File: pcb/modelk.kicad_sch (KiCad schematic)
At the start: 40 parts, among them J1 JST-PH connector, J2 Conn_01x20, J3 User exposed, J4 Conn_01x12, J5 Conn_01x04, J6 Conn_01x08, J7 Faston PCB mount, J8 Dupont for power profiling, SW1 SW_reset, U1 nice_nano, U2 74HC595, U3 74HC595, U4 74HC595

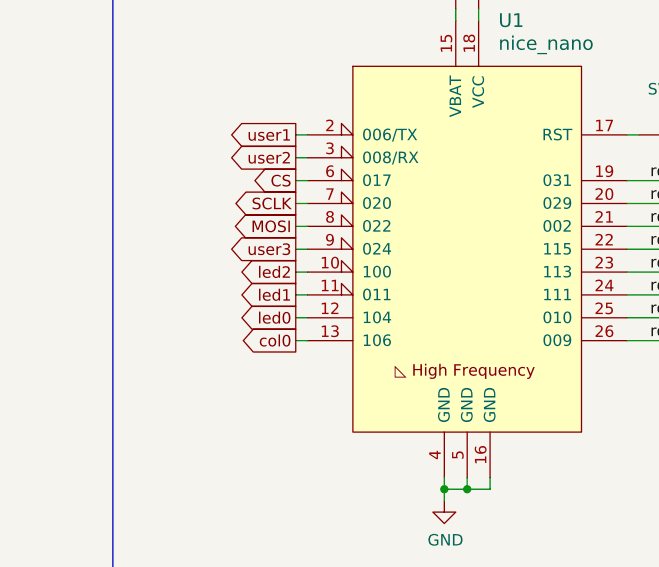
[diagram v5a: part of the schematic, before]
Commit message: All leds on high frequency pins
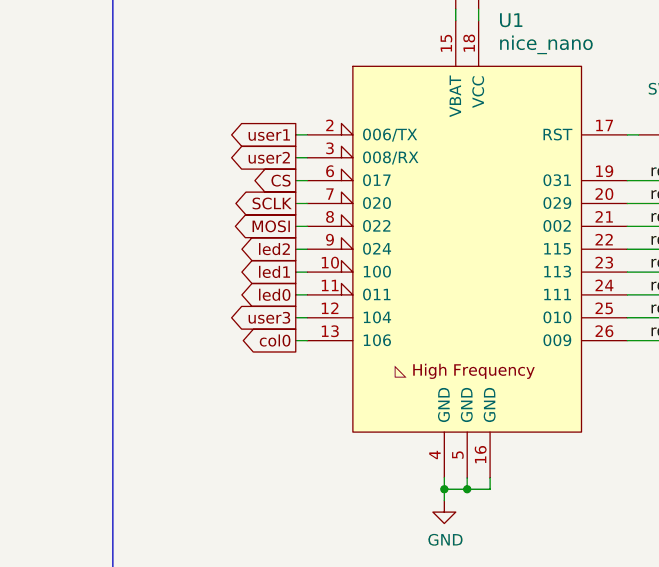
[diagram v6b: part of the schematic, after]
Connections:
- net led0: now also U1.11 (011); no longer U1.12 (104)
- net led1: now also U1.10 (100); no longer U1.11 (011)
- net led2: now also U1.9 (024); no longer U1.10 (100)
- net user3: now also U1.12 (104); no longer U1.9 (024)
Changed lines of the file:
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@@
 		(title "Model K")
 		(date "2025-06-15")
-		(rev "0.7.4")
+		(rev "0.7.5")
 	)
 	(rectangle
@@
 			"AAAAAAAAAAAAAAAAAAAAAAAAAAAAAAAAAAAAAAAAAAAAAAAAAAAAAAAAAAAAAAAAAAAAAAAAAAAA"
 			"AAAAAAAAAAAAAAAAAND29EoAAAAA0Pb0SgAAAAAAAAAAAAAAAAAAAAAAAAAAAAAAAAAAAAAAAAAA"
+			"AAAAAAAAAAAAAAAAAAAAAAAAAAAAAAAAAAAAAAAAAAAAAAAAAAAAAAAAAAAAAAAAAAAAAAAAAAAA"
+			"AAAAAAAAAAAAAAAAAAAAAAAAAAAAAAAAAAAAAAAAAAAAAAAAAAAAAAAAAAAAAAAAAAAAAAAAAAAA"
+			"AAAAAAAAAAAAAAAAAAAAAAAAAAAAAAAAAAAAAAAAAAAAAAAAAAAAAAAAAAAAAAAAAAAAAAAAAAAA"
+			"AAAAAAAAAAAAAAAAAAAAAAAAAAAAAAAAAAAAAAAAAAAAAAAAAAAAAAAAAAAAAAAAAAAAAAAAAAAA"
+			"AAAAAAAAAAAAAAAAAAAAAAAAAAAAAAAAAAAAAAAAAAAAAAAAAAAAAAAAAAAAAAAAAAAAAAAAAAAA"
+			"AAAAAAAAAAAAAAAAAAAAAAAAAAAAAAAAAAAAAAAAAAAAAAAAAAAAAAAAAAAAAAAAAAAAAAAAAAAA"
+			"AAAAAAAAAAAAAAAAAAAAAAAAAAAAAAAAAAAAAAAAAAAAAAAAAAAAAAAAAAAAAAAAAAAAAAAAAAAA"
+			"AAAAAAAAAAAAAAAAAAAAAAAAAAAAAAAAAAAAAAAAAAAAAAAAAAAAAAAAAAAAAAAAAAAAAAAAAAAA"
+			"AAAAAAAAAAAAAAAAAAAAAAAAAAAAAAAAAAAAAAAAAAAAAAAAAAAAAAAAAAAAAAAAAAAAAAAAAAAA"
+			"AAAAAAAAAAAAAAAAAAAAAAAAAAAAAAAAAAAAAAAAAAAAAAAAAAAAAAAAAAAAAAAAAAAAAAAAAAAA"
+			"AAAAAAAAAAAAAAAAAAAAAAAAAAAAAAAAAAAAAAAAAAAAAAAAAAAAAAAAAAAAAAAAAAAAAAAAAAAA"
+			"AAAAAAAAAAAAAAAAAAAAAAAAAAAAAAAAAAAAAAAAAAAAAAAAAAAAAAAAAAAAAAAAAAAAAAAAAAAA"
+			"AAAAAAAAAAAAAAAAAAAAAAAAAAAAAAAAAAAAAAAAAAAAAAAAAAAAAAAAAAAAAAAAAAAAAAAAAAAA"
+			"AAAAAAAAAAAAAAAAAAAAAAAAAAAAAAAAAAAAAAAAAAAAAAAAAAAAAAAAAAAAAAAAAAAAAAAAAAAA"
+			"AAAAAAAAAAAAAAAAAAAAAAAAAAAAAAAAAAAAAAAAAAAAAAAAAAAAAAAAAAAAAAAAAAAAAAAAAAAA"
+			"AAAAAAAAAAAAAAAAAAAAAAAAAAAAAAAAAAAAAAAAAAAAAAAAAAAAAAAAAAAAAAAAAAAAAAAAAAAA"
+			"AAAAAAAAAAAAAAAAAAAAAAAAAAAAAAAAAAAAAAAAAAAAAAAAAAAAAAAAAAAAAAAAAAAAAAAAAAAA"
+			"AAAAAAAAAAAAAAAAAAAAAAAAAAAAAAAAAAAAAAAAAAAAAAAAAAAAAAAAAAAAAAAAAAAAAAAAAAAA"
+			"AAAAAAAAAAAAAAAAAAAAAAAAAAAAAAAAAAAAAAAAAAAAAAAAAAAAAAAAAAAAAAAAAAAAAAAAAAAA"
+			"AAAAAAAAAAAAAAAAAAAAAAAAAAAAAAAAAAAAAAAAAAAAAAAAAAAAAAAAAAAAAAAAAAAAAAAAAAAA"
+			"AAAAAAAAAAAAAAAAAAAAAAAAAAAAAAAAAAAAAAAAAAAAAAAAAAAAAAAAAAAAAAAAAAAAAAAAAAAA"
+			"AAAAAAAAAAAAAAAAAAAAAAAAAAAAAAAAAAAAAAAAAAAAAAAAAAAAAAAAAAAAAAAAAAAAAAAAAAAA"
+			"AAAAAAAAAAAAAAAAAAAAAAAAAAAAAAAAAAAAAAAAAAAAAAAAAAAAAAAAAAAAAAAAAAAAAAAAAAAA"
+			"AAAAAAAAAAAAAAAAAAAAAAAAAAAAAAAAAAAAAAAAAAAAAAAAAAAAAAAAAAAAAAAAAAAAAAAAAAAA"
+			"AAAAAAAAAAAAAAAAAAAAAAAAAAAAAAAAAAAAAAAAAAAAAAAAAAAAAAAAAAAAAAAAAAAAAAAAAAAA"
+			"AAAAAAAAAAAAAAAAAAAAAAAAAAAAAAAAAAAAAAAAAAAAAAAAAAAAAAAAAAAAAAAAAAAAAAAAAAAA"
+			"AAAAAAAAAAAAAAAAAAAAAAAAAAAAAAAAAAAAAAAAAAAAAAAAAAAAAAAAAAAAAAAAAAAAAAAAAAAA"
+			"AAAAAAAAAAAAAAAAAAAAAAAAAAAAAAAAAAAAAAAAAAAAAAAAAAAAAAAAAAAAAAAAAAAAAAAAAAAA"
+			"AAAAAAAAAAAAAAAAAAAAAAAAAAAAAAAAAAAAAAAAAAAAAAAAAAAAAAAAAAAAAAAAAAAAAAAAAAAA"
+			"AAAAAAAAAAAAAAAAAAAAAAAAAAAAAAAAAAAAAAAAAAAAAAAAAAAAAAAAAAAAAAAAAAAAAAAAAAAA"
+			"AAAAAAAAAAAAAAAAAAAAAAAAAAAAAAAAAAAAAAAAAAAAAAAAAAAAAAAAAAAAAAAAAAAAAAAAAAAA"
+			"AAAAAAAAAAAAAAAAAAAAAAAAAAAAAAAAAAAAAAAAAAAAAAAAAAAAAAAAAAAAAAAAAAAAAAAAAAAA"
+			"AAAAAAAAAAAAAAAAAAAAAAAAAAAAAAAAAAAAAAAAAAAAAAAAAAAAAAAAAAAAAAAAAAAAAAAAAAAA"
+			"AAAAAAAAAAAAAAAAAAAAAAAAAAAAAAAAAAAAAAAAAAAAAAAAAAAAAAAAAAAAAAAAAAAAAAAAAAAA"
+			"AAAAAAAAAAAAAAAAAAAAAAAAAAAAAAAAAAAAAAAAAAAAAAAAAAAAAAAAAAAAAAAAAAAAAAAAAAAA"
+			"AAAAAAAAAAAAAAAAAAAAAAAAAAAAAAAAAAAAAAAAAAAAAAAAAAAAAAAAAAAAAAAAAAAAAAAAAAAA"
 			"AAAAAA=="
 		)
@@
 	(global_label "user3"
 		(shape output)
-		(at 53.34 69.85 180)
+		(at 53.34 77.47 180)
 		(effects
 			(font
@@
 		)
 		(property "Intersheetrefs" "${INTERSHEET_REFS}"
-			(at 53.34 69.85 0)
+			(at 53.34 77.47 0)
 			(effects
 				(font
@@
 	(global_label "led2"
 		(shape output)
-		(at 53.34 72.39 180)
+		(at 53.34 69.85 180)
 		(effects
 			(font
@@
 		)
 		(property "Intersheetrefs" "${INTERSHEET_REFS}"
-			(at 53.34 72.39 0)
+			(at 53.34 69.85 0)
 			(effects
 				(font
@@
 	(global_label "led0"
 		(shape output)
-		(at 53.34 77.47 180)
+		(at 53.34 74.93 180)
 		(effects
 			(font
@@
 		)
 		(property "Intersheetrefs" "${INTERSHEET_REFS}"
-			(at 53.34 77.47 0)
+			(at 53.34 74.93 0)
 			(effects
 				(font
@@
 	(global_label "led1"
 		(shape output)
-		(at 53.34 74.93 180)
+		(at 53.34 72.39 180)
 		(effects
 			(font
@@
 		)
 		(property "Intersheetrefs" "${INTERSHEET_REFS}"
-			(at 53.34 74.93 0)
+			(at 53.34 72.39 0)
 			(effects
 				(font

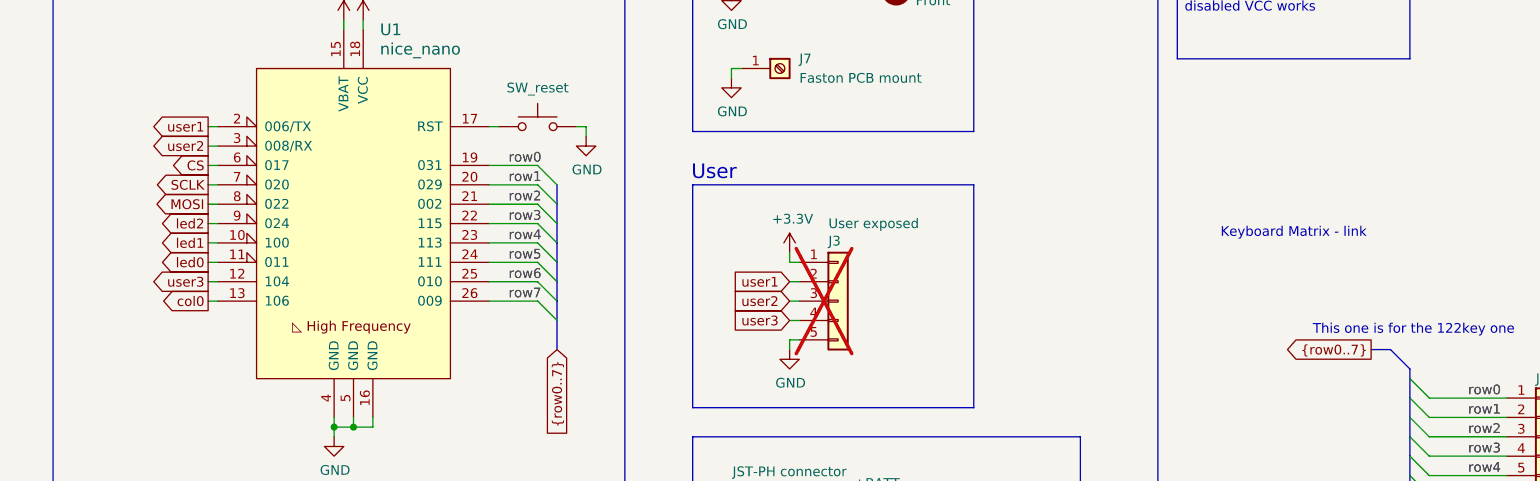
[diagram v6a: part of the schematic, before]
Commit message: Remade half the board
Redid the visual language, standardized the font and its size.
Moved diodes closer to connector.
Text is all caps now.
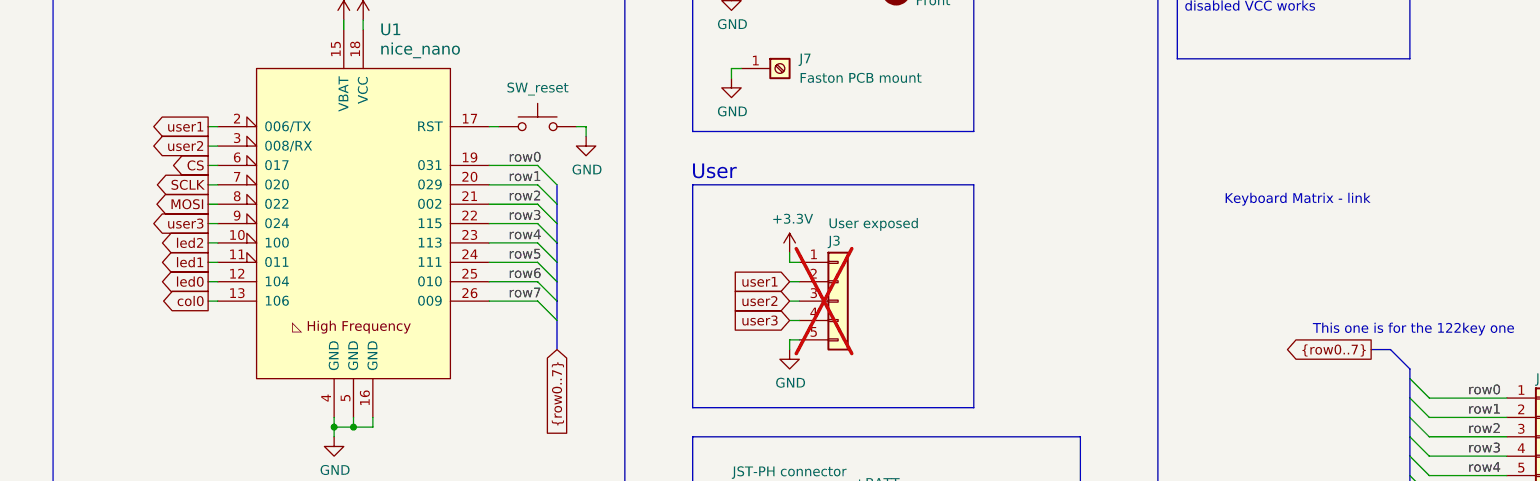
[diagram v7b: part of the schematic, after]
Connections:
- net led0: now also U1.12 (104); no longer U1.11 (011)
- net led1: now also U1.11 (011); no longer U1.10 (100)
- net led2: now also U1.10 (100); no longer U1.9 (024)
- net user3: now also U1.9 (024); no longer U1.12 (104)

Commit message: Labels
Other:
- note added: "Battery Connector"
- moved on the sheet: H1, H2, H3, H4, J3, J7, U1
